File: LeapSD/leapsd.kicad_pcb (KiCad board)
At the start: 2 copper layers, 43.8 x 33.4 mm, 11 parts

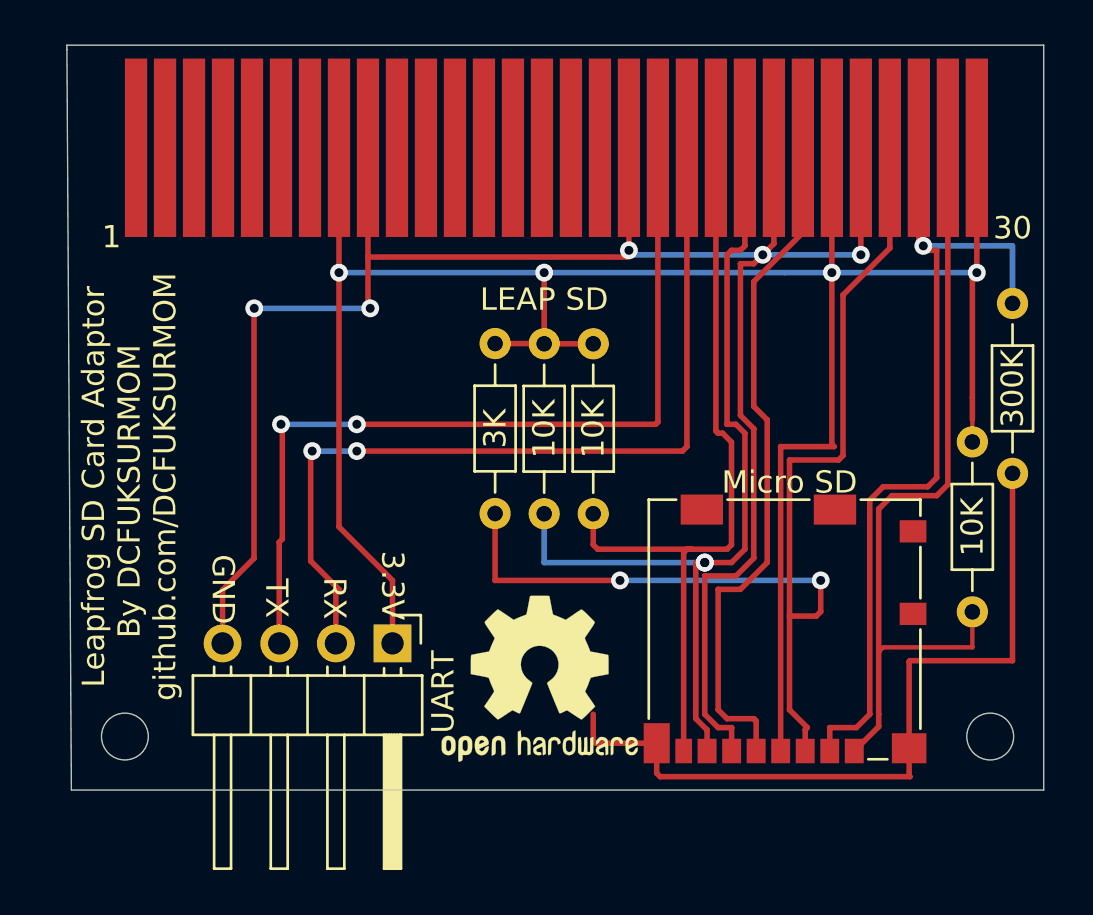
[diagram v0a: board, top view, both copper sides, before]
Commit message: Updated for LeapFlash
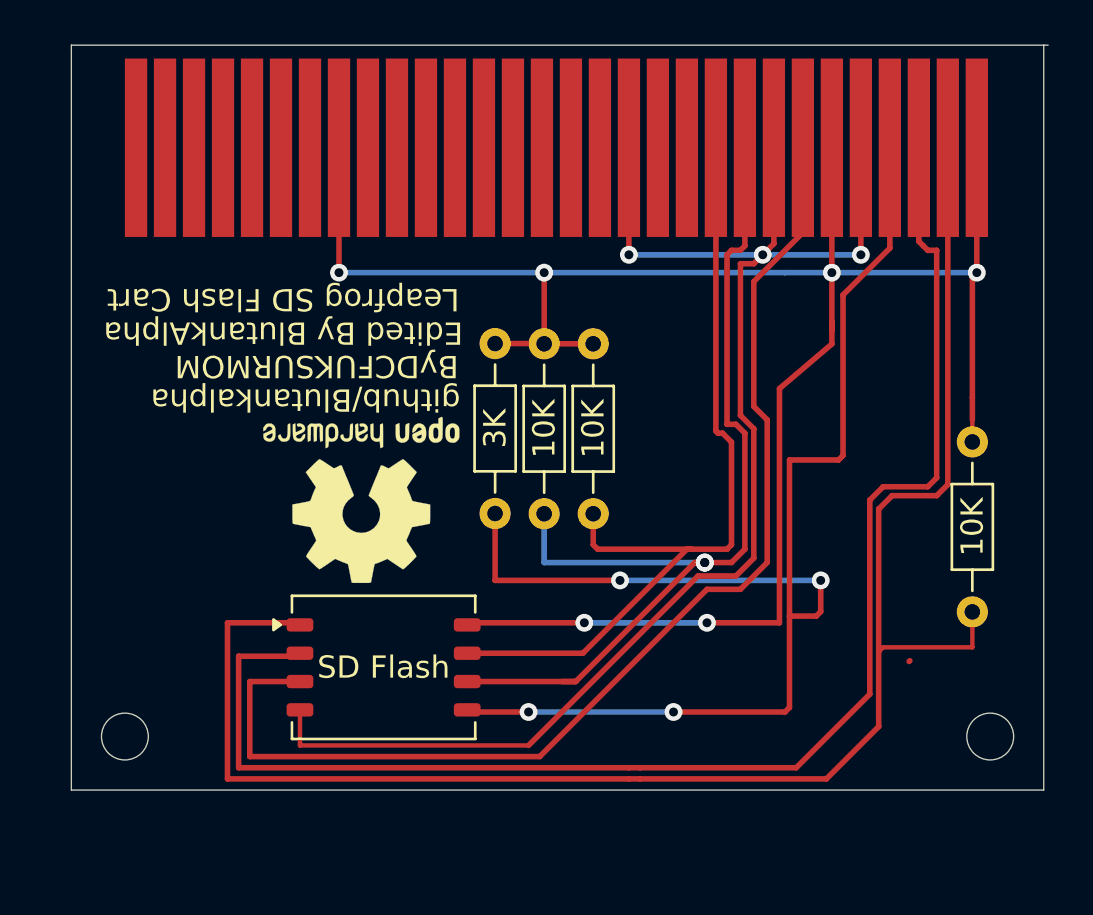
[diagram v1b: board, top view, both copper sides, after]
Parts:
- removed 300K: , Resistor_THT:R_Axial_DIN0204_L3.6mm_D1.6mm_P7.62mm_Horizontal
- removed Micro SD: microSD_HC_Molex_104031-0811, Connector_Card:microSD_HC_Molex_104031-0811
- removed UART: PinHeader_1x04_P2.54mm_Horizontal, Connector_PinHeader_2.54mm:PinHeader_1x04_P2.54mm_Horizontal
- added SD Flash: LGA-8_8x6.2mm_P1.27mm, Package_LGA:LGA-8_8x6.2mm_P1.27mm, F.Cu at (171.0, 62.5)
- moved REF** 11.3 mm to (170.0, 55.0), turned to 180 degrees
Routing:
- net (no net): track 538.6 -> 385.9 mm, vias 18 -> 15
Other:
- outline, holes or cut-outs redrawn
- board text added: "ByDCFUKSURMOM"
- board text added: "Edited By BlutankAlpha"
- board text added: "Leapfrog SD Flash Cart"
- board text added: "github/Blutankalpha"
- board text removed: "By DCFUKSURMOM"
- board text removed: "LEAP SD"
- board text removed: "Leapfrog SD Card Adaptor"
- board text removed: "github.com/DCFUKSURMOM"
